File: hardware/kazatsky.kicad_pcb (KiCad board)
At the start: 2 copper layers, 67 x 39 mm, 21 parts, among them J1 CTRL, J2 HALL, J3 VMOT, J4 MOTOR, J5 ISP, J6 USB_OTG, U1 L7805, U2 ATmega328PB-AU, U3 CH340G, Y1 12M

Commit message: Adding ADC pin for measuring input voltage.
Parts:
- added R3: 3.4k, coddingtonbear:0805_Milling, F.Cu at (182.0, 79.0)
- added R4: 10.2k, coddingtonbear:0805_Milling, F.Cu at (182.0, 77.0)
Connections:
- U2 pad 28: Net-(U2-Pad28) -> VMOT
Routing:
- net +VDC: track 13.9 -> 41.3 mm, vias 0 -> 2
- net VMOT: track 0.00 -> 19.0 mm, vias 0 -> 2
- net GND: track 221.5 -> 227.0 mm
- net USB_RESET: track 43.7 -> 45.0 mm
- net HALL: track 26.0 -> 26.9 mm

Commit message: Adding name/date/etc to board.
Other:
- board text added: "2019-10-07"
- board text added: "@coddingtonbear"
- board text added: "kazatsky desk controller"
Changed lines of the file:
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@@
   (general
     (thickness 1.6)
-    (drawings 7)
+    (drawings 10)
     (tracks 334)
     (zones 0)
@@
       (net 1 GND))
   )
+  (gr_text "kazatsky\ndesk controller" (at 152.7 86 270) (layer B.Cu)
+    (effects (font (size 1.5 1.5) (thickness 0.3)) (justify mirror))
+  )
+  (gr_text @coddingtonbear (at 213 86.6 90) (layer B.Cu)
+    (effects (font (size 1.5 1.5) (thickness 0.3)) (justify mirror))
+  )
+  (gr_text 2019-10-07 (at 213.1 86.3 90) (layer F.Cu)
+    (effects (font (size 1.5 1.5) (thickness 0.3)))
+  )
   (gr_line (start 149 67) (end 149 106) (layer Edge.Cuts) (width 0.15))

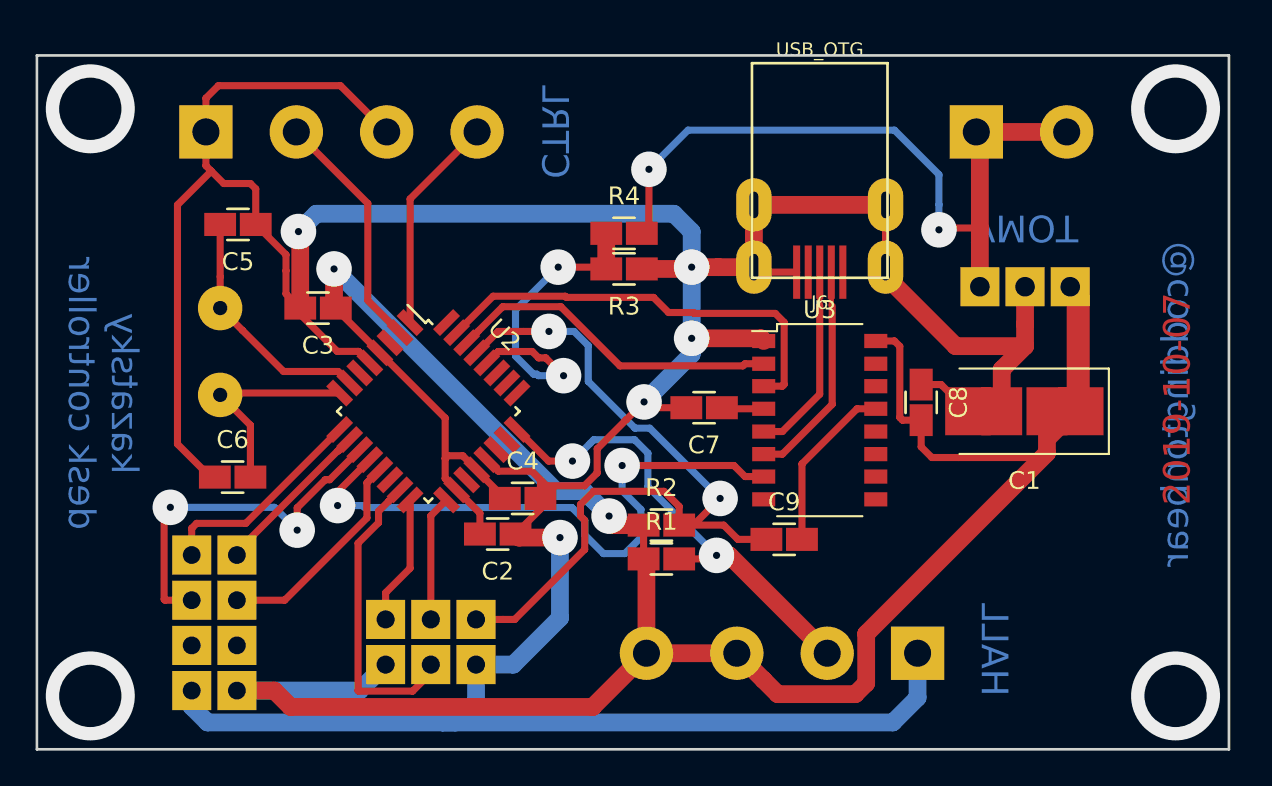
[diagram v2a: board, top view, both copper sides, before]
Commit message: Minor gnd/5v layout changes.
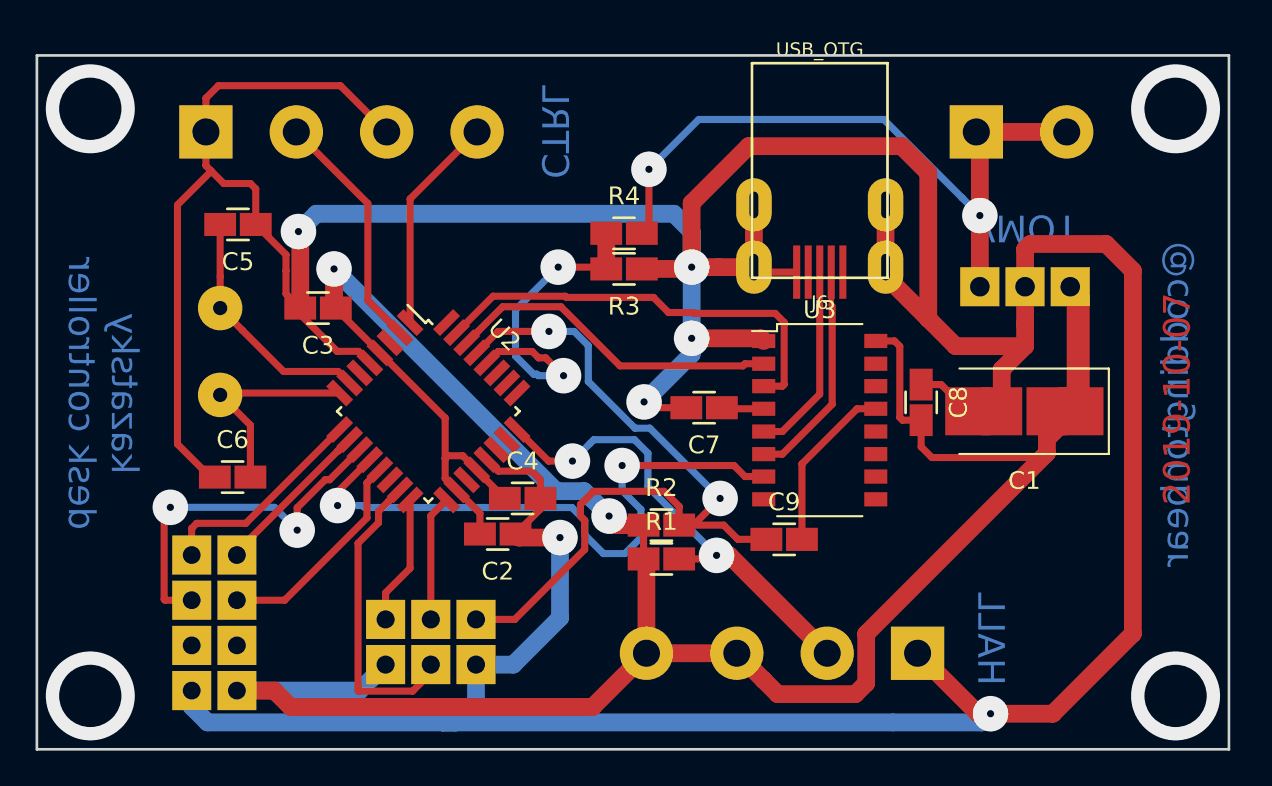
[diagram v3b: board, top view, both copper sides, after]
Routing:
- net GND: track 227.0 -> 277.0 mm, vias 5 -> 6
- net +VDC: track 41.3 -> 40.3 mm
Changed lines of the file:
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@@
     (thickness 1.6)
     (drawings 10)
-    (tracks 334)
+    (tracks 340)
     (zones 0)
     (modules 23)
@@
   )
   (setup
-    (last_trace_width 0.4)
+    (last_trace_width 1)
     (user_trace_width 1)
     (trace_clearance 0.19)
@@
   (gr_line (start 216 106) (end 216 67) (layer Edge.Cuts) (width 0.15))
   (gr_line (start 149 106) (end 216 106) (layer Edge.Cuts) (width 0.15))
-  (gr_text HALL (at 202.8 100.4 270) (layer B.Cu)
+  (gr_text HALL (at 202.6 99.8 270) (layer B.Cu)
     (effects (font (size 1.5 1.5) (thickness 0.3)) (justify mirror))
   )
@@
   (via (at 213 70) (size 5) (drill 3.5) (layers F.Cu B.Cu) (net 0))
   (via (at 213 103) (size 5) (drill 3.5) (layers F.Cu B.Cu) (net 0))
-  (segment (start 190.7 75.4) (end 196.7 75.4) (width 0.4) (layer F.Cu) (net 1))
-  (segment (start 189.3 75.4) (end 190.7 75.4) (width 0.4) (layer F.Cu) (net 1))
-  (segment (start 196.7 78.9) (end 196.7 75.4) (width 0.4) (layer F.Cu) (net 1))
   (segment (start 189.57996 79.17996) (end 189.3 78.9) (width 0.4) (layer F.Cu) (net 1))
   (segment (start 191.70206 79.17996) (end 189.57996 79.17996) (width 0.4) (layer F.Cu) (net 1))
@@
   (segment (start 200.64 83.34) (end 204.54 83.34) (width 1) (layer F.Cu) (net 1))
   (segment (start 196.7 78.9) (end 196.7 79.4) (width 1) (layer F.Cu) (net 1))
-  (segment (start 196.7 79.4) (end 200.64 83.34) (width 1) (layer F.Cu) (net 1))
-  (segment (start 196.7 75.4) (end 189.3 75.4) (width 1) (layer F.Cu) (net 1))
   (segment (start 189.3 78.9) (end 189.3 75.4) (width 1) (layer F.Cu) (net 1))
   (segment (start 172.529999 104.490001) (end 173.68 103.34) (width 1) (layer B.Cu) (net 1))
@@
   (segment (start 173.68 103.34) (end 173.68 101.24) (width 1) (layer B.Cu) (net 1))
   (segment (start 157.7 103.602002) (end 158.587999 104.490001) (width 1) (layer B.Cu) (net 1))
-  (segment (start 197.109999 104.490001) (end 198.5 103.1) (width 1) (layer B.Cu) (net 1))
   (segment (start 171.8 104.490001) (end 197.109999 104.490001) (width 1) (layer B.Cu) (net 1))
-  (segment (start 198.5 103.1) (end 198.5 100.6) (width 1) (layer B.Cu) (net 1))
   (segment (start 158.587999 104.490001) (end 171.8 104.490001) (width 1) (layer B.Cu) (net 1))
   (segment (start 171.8 104.490001) (end 172.529999 104.490001) (width 1) (layer B.Cu) (net 1))
@@
   (segment (start 185.7 79) (end 185.8 78.9) (width 1) (layer F.Cu) (net 1))
   (segment (start 183 79) (end 185.7 79) (width 1) (layer F.Cu) (net 1))
-  (segment (start 180.490002 89.109998) (end 182.125313 87.474687) (width 0.4) (layer F.Cu) (net 1))
-  (segment (start 177.3 90.85) (end 177.640002 91.190002) (width 0.4) (layer F.Cu) (net 1))
-  (segment (start 179.767202 91.190002) (end 180.490002 90.467202) (width 0.4) (layer F.Cu) (net 1))
-  (segment (start 177.640002 91.190002) (end 179.767202 91.190002) (width 0.4) (layer F.Cu) (net 1))
-  (segment (start 182.125313 87.474687) (end 183.125312 86.474688) (width 0.4) (layer F.Cu) (net 1))
-  (segment (start 180.490002 90.467202) (end 180.490002 89.109998) (width 0.4) (layer F.Cu) (net 1))
   (via (at 163.7 76.9) (size 2) (drill 0.4) (layers F.Cu B.Cu) (net 1))
   (segment (start 163.8 81.2) (end 163.8 77) (width 1) (layer F.Cu) (net 1))
@@
   (segment (start 185.8 76.9) (end 185.8 78.9) (width 1) (layer B.Cu) (net 1))
   (segment (start 184.800001 75.900001) (end 185.8 76.9) (width 1) (layer B.Cu) (net 1))
+  (via (at 202.6 104) (size 2) (drill 0.4) (layers F.Cu B.Cu) (net 1))
+  (segment (start 197.109999 104.490001) (end 202.109999 104.490001) (width 1) (layer B.Cu) (net 1))
+  (segment (start 202.109999 104.490001) (end 202.6 104) (width 1) (layer B.Cu) (net 1))
+  (segment (start 201.9 104) (end 198.5 100.6) (width 1) (layer F.Cu) (net 1))
+  (segment (start 202.6 104) (end 201.9 104) (width 1) (layer F.Cu) (net 1))
+  (segment (start 204.84 77.6) (end 204.54 77.9) (width 1) (layer F.Cu) (net 1))
+  (segment (start 202.6 104) (end 206.1 104) (width 1) (layer F.Cu) (net 1))
+  (segment (start 210.6 99.5) (end 210.6 79.1) (width 1) (layer F.Cu) (net 1))
+  (segment (start 204.54 77.9) (end 204.54 80) (width 1) (layer F.Cu) (net 1))
+  (segment (start 206.1 104) (end 210.6 99.5) (width 1) (layer F.Cu) (net 1))
+  (segment (start 210.6 79.1) (end 209.1 77.6) (width 1) (layer F.Cu) (net 1))
+  (segment (start 209.1 77.6) (end 204.84 77.6) (width 1) (layer F.Cu) (net 1))
+  (segment (start 196.7 75.4) (end 196.7 74.9) (width 1) (layer F.Cu) (net 1))
+  (segment (start 199.1 73.6) (end 199.1 81.8) (width 1) (layer F.Cu) (net 1))
+  (segment (start 197.6 72.1) (end 199.1 73.6) (width 1) (layer F.Cu) (net 1))
+  (segment (start 199.1 81.8) (end 200.64 83.34) (width 1) (layer F.Cu) (net 1))
+  (segment (start 185.8 75.3) (end 189 72.1) (width 1) (layer F.Cu) (net 1))
+  (segment (start 185.8 78.9) (end 185.8 75.3) (width 1) (layer F.Cu) (net 1))
+  (segment (start 196.7 79.4) (end 199.1 81.8) (width 1) (layer F.Cu) (net 1))
+  (segment (start 189 72.1) (end 197.6 72.1) (width 1) (layer F.Cu) (net 1))
+  (segment (start 196.7 78.9) (end 196.7 75.4) (width 1) (layer F.Cu) (net 1))
   (segment (start 161 87.78) (end 159.3 86.08) (width 0.4) (layer F.Cu) (net 4))
   (segment (start 161 90.7) (end 161 87.78) (width 0.4) (layer F.Cu) (net 4))
@@
   (segment (start 202 71.5) (end 201.8 71.3) (width 1) (layer F.Cu) (net 13))
   (segment (start 206.88 71.3) (end 201.8 71.3) (width 1) (layer F.Cu) (net 13))
-  (via (at 199.7 76.8) (size 2) (drill 0.4) (layers F.Cu B.Cu) (net 13))
-  (segment (start 202 76.7) (end 199.8 76.7) (width 0.4) (layer F.Cu) (net 13))
-  (segment (start 199.8 76.7) (end 199.7 76.8) (width 0.4) (layer F.Cu) (net 13))
   (segment (start 202 80) (end 202 76.7) (width 1) (layer F.Cu) (net 13))
   (segment (start 202 76.7) (end 202 71.5) (width 1) (layer F.Cu) (net 13))
-  (segment (start 199.7 76.8) (end 199.7 75.385787) (width 0.4) (layer B.Cu) (net 13))
-  (segment (start 199.7 75.385787) (end 199.7 73.7) (width 0.4) (layer B.Cu) (net 13))
-  (segment (start 199.7 73.7) (end 197.2 71.2) (width 0.4) (layer B.Cu) (net 13))
-  (segment (start 197.2 71.2) (end 185.6 71.2) (width 0.4) (layer B.Cu) (net 13))
   (via (at 183.4 73.4) (size 2) (drill 0.4) (layers F.Cu B.Cu) (net 13))
-  (segment (start 185.6 71.2) (end 183.4 73.4) (width 0.4) (layer B.Cu) (net 13))
   (segment (start 183.4 76.6) (end 183 77) (width 0.4) (layer F.Cu) (net 13))
   (segment (start 183.4 73.4) (end 183.4 76.6) (width 0.4) (layer F.Cu) (net 13))
+  (segment (start 202 76.7) (end 202 76) (width 0.4) (layer F.Cu) (net 13))
+  (via (at 202 76) (size 2) (drill 0.4) (layers F.Cu B.Cu) (net 13))
+  (segment (start 201.000001 75.000001) (end 202 76) (width 0.4) (layer B.Cu) (net 13))
+  (segment (start 196.6 70.6) (end 201.000001 75.000001) (width 0.4) (layer B.Cu) (net 13))
+  (segment (start 183.4 73.4) (end 186.2 70.6) (width 0.4) (layer B.Cu) (net 13))
+  (segment (start 186.2 70.6) (end 196.6 70.6) (width 0.4) (layer B.Cu) (net 13))
   (segment (start 188.8 84.33) (end 188.679999 84.450001) (width 0.4) (layer F.Cu) (net 14))
   (segment (start 188.679999 84.450001) (end 181.774165 84.450001) (width 0.4) (layer F.Cu) (net 14))

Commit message: Updating to v2.0 of the board.
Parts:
- removed C5, C6: 22p, coddingtonbear:0805_Milling
- removed J5: ISP, Connector_IDC:IDC-Header_2x03_P2.54mm_Vertical
- removed R1: 10k, coddingtonbear:0805_Milling
- removed Y1: 12M, coddingtonbear:Crystal_HC49-U_Vertical_LargePads
- J2: value HALL -> HALL/LIMIT/RST; footprint TerminalBlock:TerminalBlock_bornier-4_P5.08mm -> TerminalBlock_RND:TerminalBlock_RND_205-00238_1x08_P5.08mm_Horizontal
- U3: value CH340G -> CH340B; footprint Package_SO:SOP-16_4.4x10.4mm_P1.27mm -> Package_SO:SOIC-16_4.55x10.3mm_P1.27mm
- moved J2 5.61 mm to (204.1, 101.0)
- moved R2 2.98 mm to (187.0, 92.7), turned to 270 degrees
- moved C9 2.12 mm to (193.1, 94.5), turned to 180 degrees
- moved U3 0.10 mm to (193.0, 87.4)
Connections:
- C9 pad 1: USB_RESET -> USB_RESET_DTR
- J2 pad 1: GND -> USB_RESET_DTR
- J2 pad 2: HALL -> USB_RESET
- J2 pad 3: +5V -> Net-(J2-Pad3)
- J2 pad 4: +5V -> ~LIMIT
- J4 pad 3: Net-(J4-Pad3) -> (no net)
- J4 pad 4: Net-(J4-Pad4) -> (no net)
- J6 pad 1: Net-(J6-Pad1) -> (no net)
- J6 pad 4: Net-(J6-Pad4) -> (no net)
- U2 pad 11: L_EN -> (no net)
- U2 pad 12: Net-(U2-Pad12) -> (no net)
- U2 pad 14: Net-(U2-Pad14) -> (no net)
- U2 pad 15: MOSI -> (no net)
- U2 pad 16: MISO -> (no net)
- U2 pad 17: SCK -> (no net)
- U2 pad 19: Net-(U2-Pad19) -> (no net)
- U2 pad 22: Net-(U2-Pad22) -> (no net)
- U2 pad 23: Net-(U2-Pad23) -> HALL
- U2 pad 24: HALL -> ~LIMIT
- U2 pad 25: Net-(U2-Pad25) -> Net-(J2-Pad3)
- U2 pad 26: Net-(U2-Pad26) -> (no net)
- U2 pad 27: Net-(U2-Pad27) -> (no net)
- U2 pad 28: VMOT -> (no net)
- U2 pad 3: Net-(U2-Pad3) -> (no net)
- U2 pad 32: Net-(U2-Pad32) -> VMOT
- U2 pad 6: Net-(U2-Pad6) -> L_EN
- U2 pad 7: Net-(C5-Pad2) -> (no net)
- U2 pad 8: Net-(C6-Pad2) -> (no net)
- U3 pad 10: Net-(U3-Pad10) -> (no net)
- U3 pad 11: Net-(U3-Pad11) -> (no net)
- U3 pad 12: Net-(U3-Pad12) -> (no net)
- U3 pad 14: Net-(U3-Pad14) -> (no net)
- U3 pad 15: Net-(U3-Pad15) -> (no net)
- U3 pad 7: Net-(U2-Pad12) -> (no net)
- U3 pad 8: Net-(U3-Pad8) -> (no net)
- U3 pad 9: Net-(U3-Pad9) -> (no net)
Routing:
- net GND: track 277.0 -> 204.4 mm, vias 6 -> 4
- net +5V: track 169.0 -> 128.9 mm, vias 2 -> 3
- net Net-(U2-Pad12): track 35.0 -> 0.00 mm, vias 2 -> 0
- net Net-(J2-Pad3): track 0.00 -> 25.9 mm
- net ~LIMIT: track 0.00 -> 19.4 mm
- net MOSI: track 17.3 -> 0.00 mm
- net Net-(C5-Pad2): track 13.7 -> 0.00 mm
- net USB_RESET_DTR: track 0.00 -> 12.7 mm
- net Net-(C6-Pad2): track 12.1 -> 0.00 mm
- net HALL: track 26.9 -> 16.2 mm, vias 2 -> 0
- net USB_RESET: track 45.0 -> 35.1 mm, vias 2 -> 0
- net MISO: track 7.28 -> 0.00 mm
- net SCK: track 7.08 -> 0.00 mm
- net VMOT: track 19.0 -> 12.2 mm, vias 2 -> 0
- net L_EN: track 20.7 -> 23.4 mm, vias 2 -> 0
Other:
- board text added: "2021-02-26"
- board text added: "STATUS"
- board text removed: "2019-10-07"
- board text removed: "HALL"

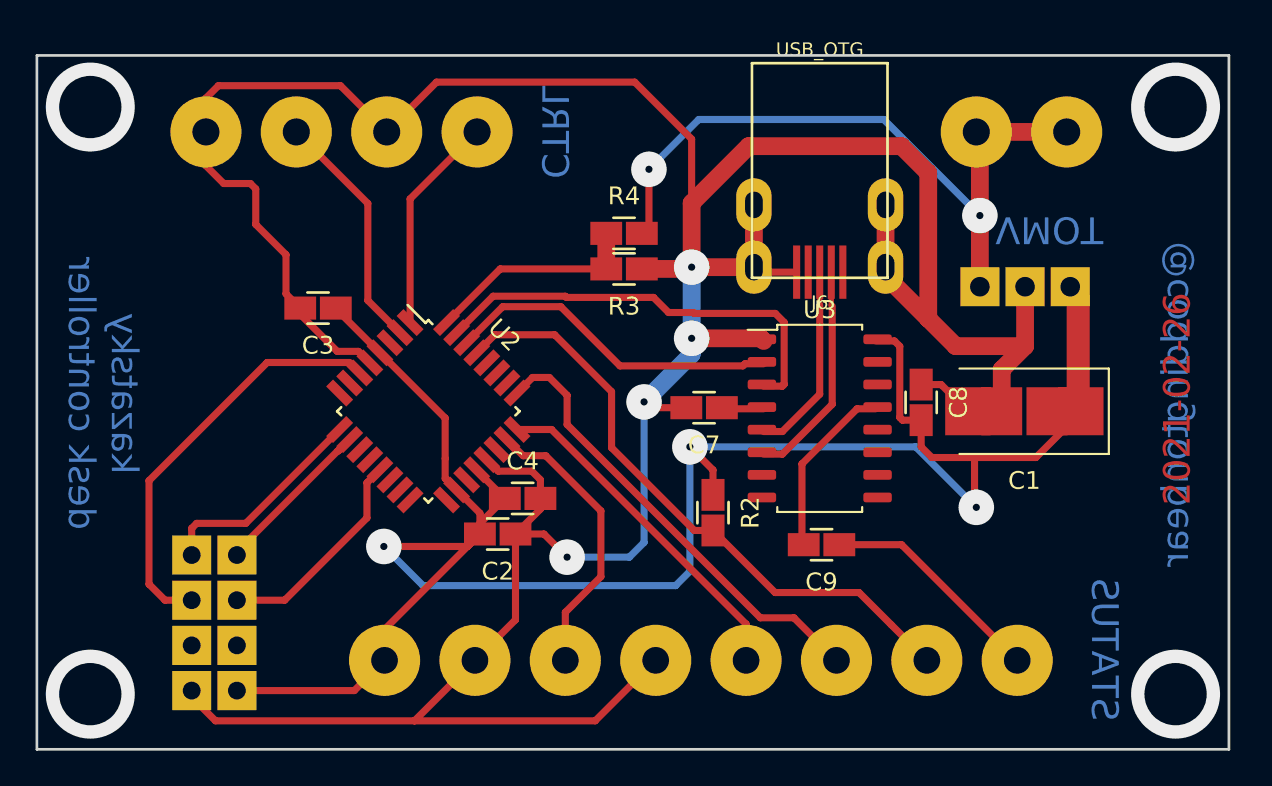
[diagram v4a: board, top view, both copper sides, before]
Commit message: Adding extra capacitance.
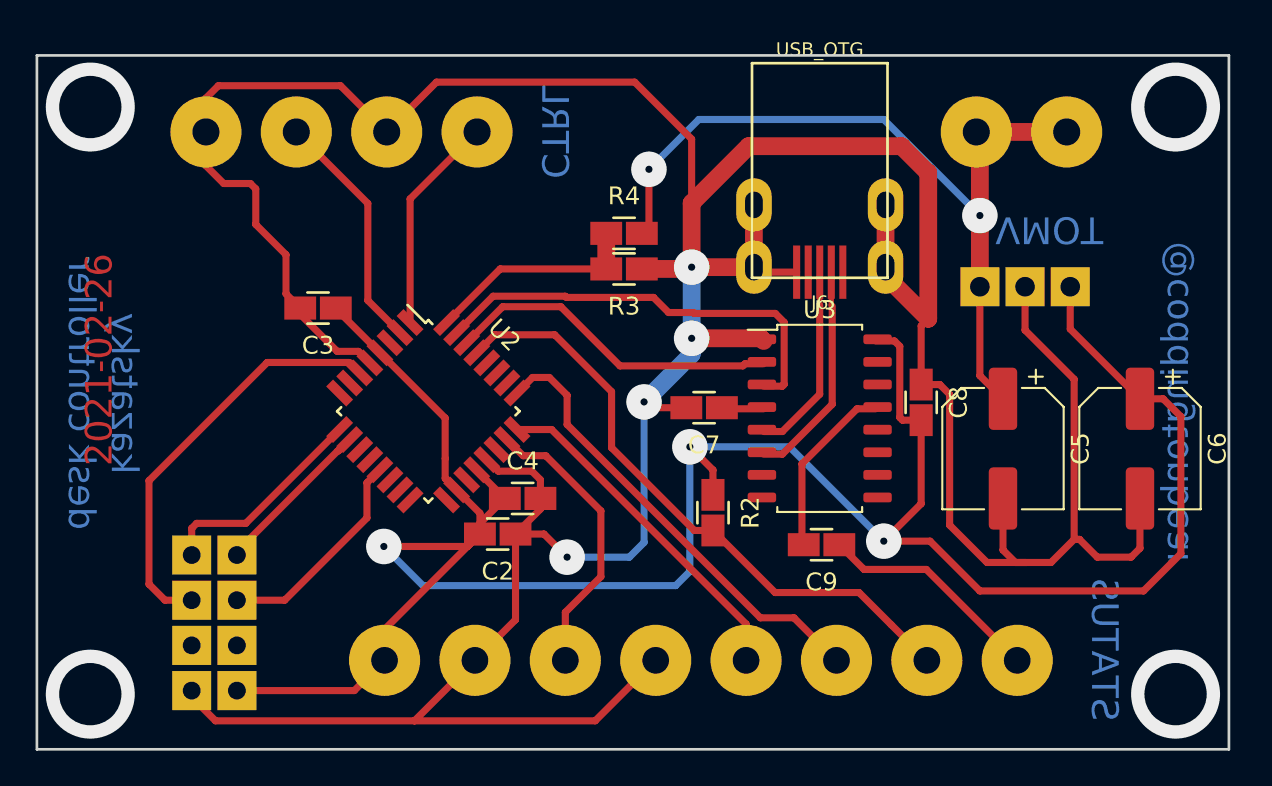
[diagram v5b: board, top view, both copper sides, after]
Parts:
- removed C1: 10u, coddingtonbear:CP_Tantalum_Case-D_EIA-7343-31_Milling
- added C5: 100u, Capacitor_SMD:CP_Elec_6.3x5.4, F.Cu at (203.3, 89.1)
- added C6: 100u, Capacitor_SMD:CP_Elec_6.3x5.4, F.Cu at (211.0, 89.1)
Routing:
- net GND: track 204.4 -> 234.0 mm
- net +5V: track 128.9 -> 138.2 mm
- net +VDC: track 40.3 -> 47.2 mm

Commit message: Updating board version/date.
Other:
- board text added: "2.0"
- board text added: "2021-02-28"
- board text removed: "2021-02-26"
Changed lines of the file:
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@@
   (general
     (thickness 1.6)
-    (drawings 10)
+    (drawings 11)
     (tracks 235)
     (zones 0)
@@
     (add_net L_EN)
     (add_net L_PWM)
-    (add_net MISO)
-    (add_net MOSI)
     (add_net "Net-(C7-Pad1)")
     (add_net "Net-(C9-Pad2)")
     (add_net "Net-(J2-Pad3)")
-    (add_net "Net-(J4-Pad3)")
-    (add_net "Net-(J4-Pad4)")
-    (add_net "Net-(J6-Pad1)")
-    (add_net "Net-(J6-Pad4)")
-    (add_net "Net-(U2-Pad11)")
-    (add_net "Net-(U2-Pad12)")
-    (add_net "Net-(U2-Pad14)")
-    (add_net "Net-(U2-Pad19)")
-    (add_net "Net-(U2-Pad22)")
-    (add_net "Net-(U2-Pad26)")
-    (add_net "Net-(U2-Pad27)")
-    (add_net "Net-(U2-Pad28)")
-    (add_net "Net-(U2-Pad3)")
-    (add_net "Net-(U2-Pad7)")
-    (add_net "Net-(U2-Pad8)")
-    (add_net "Net-(U3-Pad10)")
-    (add_net "Net-(U3-Pad11)")
-    (add_net "Net-(U3-Pad12)")
-    (add_net "Net-(U3-Pad14)")
-    (add_net "Net-(U3-Pad15)")
-    (add_net "Net-(U3-Pad7)")
-    (add_net "Net-(U3-Pad8)")
-    (add_net "Net-(U3-Pad9)")
     (add_net RXD)
     (add_net R_EN)
     (add_net R_PWM)
-    (add_net SCK)
     (add_net TXD)
     (add_net USB_RESET)
@@
     )
   )
+  (gr_text 2.0 (at 157.7 81.1) (layer F.Cu)
+    (effects (font (size 3 3) (thickness 0.75)))
+  )
   (gr_text "kazatsky\ndesk controller" (at 152.7 86 270) (layer B.Cu)
     (effects (font (size 1.5 1.5) (thickness 0.3)) (justify mirror))
@@
     (effects (font (size 1.5 1.5) (thickness 0.3)) (justify mirror))
   )
-  (gr_text 2021-02-26 (at 152.5 84.1 90) (layer F.Cu)
+  (gr_text 2021-02-28 (at 152.5 84.1 90) (layer F.Cu)
     (effects (font (size 1.5 1.5) (thickness 0.3)))
   )
